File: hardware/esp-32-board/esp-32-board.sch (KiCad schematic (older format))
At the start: 12 parts, among them J1 MainConnector, J2 Conn_01x06, J3 ESP-PROG-Program, J4 ESP-PROG-Debug, SW1 SW_Push, SW2 SW_Push, U1 ESP32-WROOM-32

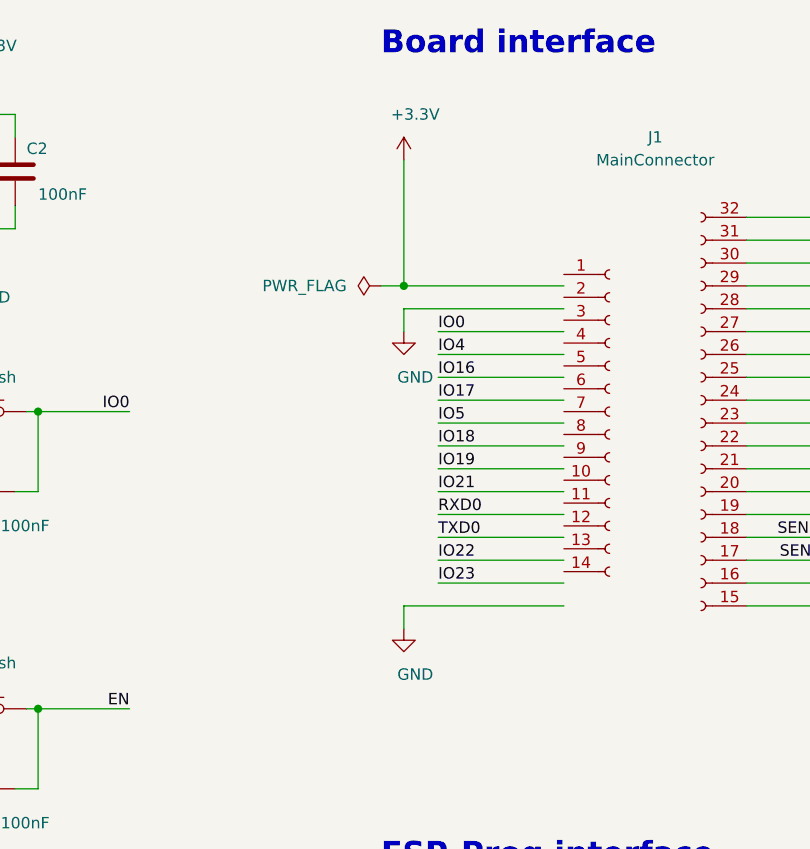
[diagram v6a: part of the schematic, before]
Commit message: Replace 15-pin header with 14-pin one
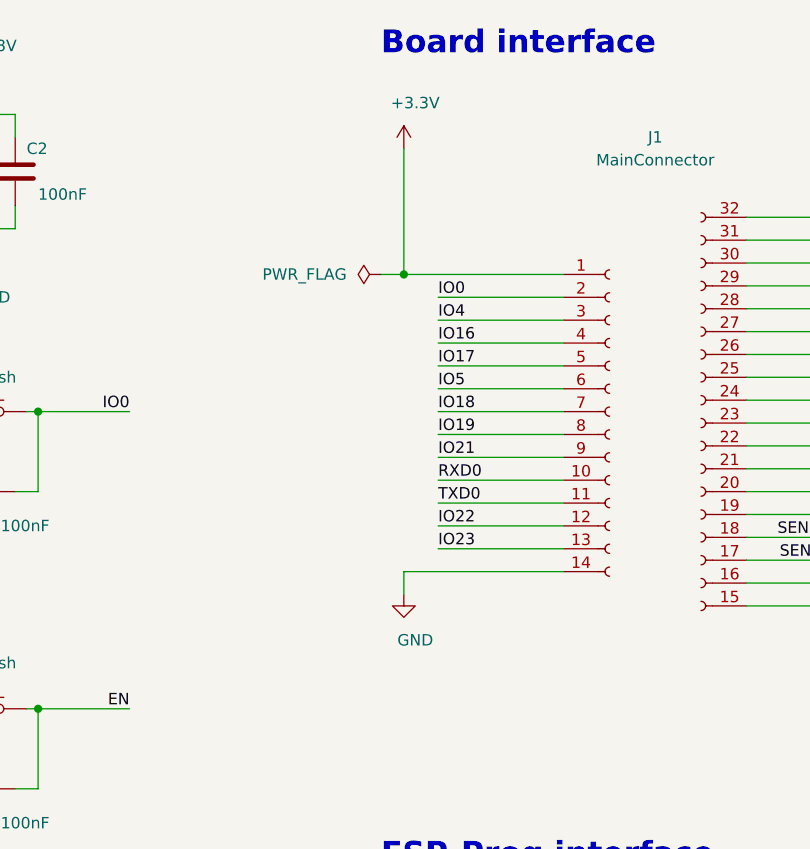
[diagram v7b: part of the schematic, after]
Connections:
- wire segments 135 -> 133
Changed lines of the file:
@@
 	1    0    0    -1
 $EndComp
-Text Label 6850 3350 0    50   ~ 0
+Text Label 6850 3200 0    50   ~ 0
 IO23
-Text Label 6850 3250 0    50   ~ 0
+Text Label 6850 3100 0    50   ~ 0
 IO22
-Text Label 6850 3150 0    50   ~ 0
+Text Label 6850 3000 0    50   ~ 0
 TXD0
-Text Label 6850 3050 0    50   ~ 0
+Text Label 6850 2900 0    50   ~ 0
 RXD0
-Text Label 6850 2950 0    50   ~ 0
+Text Label 6850 2800 0    50   ~ 0
 IO21
-Text Label 6850 2850 0    50   ~ 0
+Text Label 6850 2700 0    50   ~ 0
 IO19
-Text Label 6850 2750 0    50   ~ 0
+Text Label 6850 2600 0    50   ~ 0
 IO18
-Text Label 6850 2650 0    50   ~ 0
+Text Label 6850 2500 0    50   ~ 0
 IO5
-Text Label 6850 2550 0    50   ~ 0
+Text Label 6850 2400 0    50   ~ 0
 IO17
-Text Label 6850 2450 0    50   ~ 0
+Text Label 6850 2300 0    50   ~ 0
 IO16
-Text Label 6850 2350 0    50   ~ 0
+Text Label 6850 2200 0    50   ~ 0
 IO4
-Text Label 6850 2250 0    50   ~ 0
+Text Label 6850 2100 0    50   ~ 0
 IO0
 Text Label 8750 1950 2    50   ~ 0
@@
 CLK
 Wire Wire Line
-	7400 3350 6850 3350
-Wire Wire Line
-	7400 3250 6850 3250
-Wire Wire Line
-	7400 3150 6850 3150
-Wire Wire Line
-	7400 3050 6850 3050
-Wire Wire Line
-	7400 2850 6850 2850
-Wire Wire Line
-	7400 2750 6850 2750
-Wire Wire Line
-	7400 2650 6850 2650
-Wire Wire Line
-	7400 2450 6850 2450
-Wire Wire Line
-	6850 2350 7400 2350
-Wire Wire Line
-	7400 2250 6850 2250
+	7400 3200 6850 3200
+Wire Wire Line
+	7400 3100 6850 3100
+Wire Wire Line
+	7400 3000 6850 3000
+Wire Wire Line
+	7400 2900 6850 2900
+Wire Wire Line
+	7400 2700 6850 2700
+Wire Wire Line
+	7400 2600 6850 2600
+Wire Wire Line
+	7400 2500 6850 2500
+Wire Wire Line
+	7400 2300 6850 2300
+Wire Wire Line
+	6850 2200 7400 2200
+Wire Wire Line
+	7400 2100 6850 2100
 Wire Wire Line
 	8200 2050 8750 2050
@@
 	8750 2850 8200 2850
 Wire Wire Line
-	7400 2950 6850 2950
-Wire Wire Line
-	7400 2550 6850 2550
+	7400 2800 6850 2800
+Wire Wire Line
+	7400 2400 6850 2400
 $Comp
 L Connector:ESP-PROG-Program J3
@@
 L power:+3.3V #PWR011
 U 1 1 6028A651
-P 6700 1500
-F 0 "#PWR011" H 6700 1350 50  0001 C CNN
-F 1 "+3.3V" H 6750 1700 50  0000 C CNN
-F 2 "" H 6700 1500 50  0001 C CNN
-F 3 "" H 6700 1500 50  0001 C CNN
-	1    6700 1500
-	1    0    0    -1
-$EndComp
-Wire Wire Line
-	6700 2050 6700 1500
-Wire Wire Line
-	6700 2050 7400 2050
+P 6700 1450
+F 0 "#PWR011" H 6700 1300 50  0001 C CNN
+F 1 "+3.3V" H 6750 1650 50  0000 C CNN
+F 2 "" H 6700 1450 50  0001 C CNN
+F 3 "" H 6700 1450 50  0001 C CNN
+	1    6700 1450
+	1    0    0    -1
+$EndComp
+Wire Wire Line
+	6700 2000 6700 1450
+Wire Wire Line
+	6700 2000 7400 2000
 $Comp
 L Connector_Generic:Conn_01x06 J2
@@
 F4 "TXD0" I L 1250 6450 50
 F5 "RXD0" O L 1250 6600 50
-F7 "+5V" U R 2300 6400 50
+F6 "+5V" U R 2300 6400 50
 $EndSheet
 Text Label 2600 6800 2    50   ~ 0
@@
 L power:PWR_FLAG #FLG0103
 U 1 1 5FD0B643
-P 6600 2050
-F 0 "#FLG0103" H 6600 2125 50  0001 C CNN
-F 1 "PWR_FLAG" V 6600 2200 50  0000 L CNN
-F 2 "" H 6600 2050 50  0001 C CNN
-F 3 "~" H 6600 2050 50  0001 C CNN
-	1    6600 2050
+P 6600 2000
+F 0 "#FLG0103" H 6600 2075 50  0001 C CNN
+F 1 "PWR_FLAG" V 6600 2150 50  0000 L CNN
+F 2 "" H 6600 2000 50  0001 C CNN
+F 3 "~" H 6600 2000 50  0001 C CNN
+	1    6600 2000
 	0    -1   -1   0
 $EndComp
 Wire Wire Line
-	6600 2050 6700 2050
-Connection ~ 6700 2050
+	6600 2000 6700 2000
+Connection ~ 6700 2000
 Wire Wire Line
 	2100 4400 2100 4500
-$Comp
-L power:GND #PWR0101
-U 1 1 5FF57139
-P 6700 2250
-F 0 "#PWR0101" H 6700 2000 50  0001 C CNN
-F 1 "GND" H 6750 2050 50  0000 C CNN
-F 2 "" H 6700 2250 50  0001 C CNN
-F 3 "" H 6700 2250 50  0001 C CNN
-	1    6700 2250
-	1    0    0    -1
-$EndComp
-Wire Wire Line
-	7400 2150 6700 2150
-Wire Wire Line
-	6700 2150 6700 2250
-Wire Wire Line
-	6700 3450 7400 3450
-Wire Wire Line
-	6700 3450 6700 3550
+Wire Wire Line
+	6700 3300 7400 3300
+Wire Wire Line
+	6700 3300 6700 3400
 $Comp
 L power:GND #PWR012
 U 1 1 5FC02DF9
-P 6700 3550
-F 0 "#PWR012" H 6700 3300 50  0001 C CNN
-F 1 "GND" H 6750 3350 50  0000 C CNN
-F 2 "" H 6700 3550 50  0001 C CNN
-F 3 "" H 6700 3550 50  0001 C CNN
-	1    6700 3550
-	1    0    0    -1
-$EndComp
+P 6700 3400
+F 0 "#PWR012" H 6700 3150 50  0001 C CNN
+F 1 "GND" H 6750 3200 50  0000 C CNN
+F 2 "" H 6700 3400 50  0001 C CNN
+F 3 "" H 6700 3400 50  0001 C CNN
+	1    6700 3400
+	1    0    0    -1
+$EndComp

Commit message: Replace power switch with jumper, add RX/TX leds
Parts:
- J2: VendorLink (none) -> https://www.tme.eu/pl/details/zl262-6sg/listwy-i-gniazda-ko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
- J3: VendorLink (none) -> https://www.ebay.com/itm/10Pcs-1-27mm-Pitch-2x3-Pin-6-Pin-S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
- J4: VendorLink (none) -> https://www.ebay.com/itm/5Pcs-1-27mm-Pitch-2x5-Pin-10-Pin-S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
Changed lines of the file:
@@
 F 2 "Connector_IDC:IDC-Header_2x03_P1.27mm_Vertical_SMD" V 6850 5650 50  0001 C CNN
 F 3 "https://github.com/espressif/esp-iot-solution/blob/master/documents/evaluation_boards/ESP-Prog_guide_en.md" H 5825 5050 50  0001 C CNN
+F 4 "https://www.ebay.com/itm/10Pcs-1-27mm-Pitch-2x3-Pin-6-Pin-SMT-SMD-Male-Shrouded-Box-Header-IDC-Connector/183523538792?hash=item2abadaf768:g:-H4AAOSwm-Fb4s52" H 7100 5600 50  0001 C CNN "VendorLink"
 	1    7100 5600
 	1    0    0    -1
@@
 F 2 "Connector_IDC:IDC-Header_2x05_P1.27mm_Vertical_SMD" V 8850 5650 50  0001 C CNN
 F 3 "https://github.com/espressif/esp-iot-solution/blob/master/documents/evaluation_boards/ESP-Prog_guide_en.md" H 7825 5050 50  0001 C CNN
+F 4 "https://www.ebay.com/itm/5Pcs-1-27mm-Pitch-2x5-Pin-10-Pin-SMT-SMD-Male-Shrouded-Box-Header-IDC-Connector/172311876086?hash=item281e9691f6:g:eHIAAOSwu6taWHc7" H 9100 5600 50  0001 C CNN "VendorLink"
 	1    9100 5600
 	1    0    0    -1
@@
 F 3 "~" H 10000 2450 50  0001 C CNN
 F 4 "N/A" H 10000 2450 50  0001 C CNN "Vendor"
+F 5 "https://www.tme.eu/pl/details/zl262-6sg/listwy-i-gniazda-kolkowe/connfly/ds1023-1-6s21/" H 10000 2450 50  0001 C CNN "VendorLink"
 	1    10000 2450
 	1    0    0    -1
